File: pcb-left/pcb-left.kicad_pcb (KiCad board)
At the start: 2 copper layers, 138.1 x 95.3 mm, 80 parts, among them SW1 SW_Push, U1 ATmega32U4-AU, Y1 16MHz

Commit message: finished left side pcb
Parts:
- moved C3 1.08 mm to (97.2, 125.4)
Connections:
- U1 pad 10: Net-(U1-Pad10) -> row2
- U1 pad 11: Net-(U1-Pad11) -> row1
- U1 pad 12: Net-(U1-Pad12) -> col6
- U1 pad 18: Net-(U1-Pad18) -> SD+
- U1 pad 19: Net-(U1-Pad19) -> SD-
- U1 pad 20: Net-(U1-Pad20) -> col3
- U1 pad 21: Net-(U1-Pad21) -> col4
- U1 pad 22: Net-(U1-Pad22) -> col5
- U1 pad 29: Net-(U1-Pad29) -> row4
- U1 pad 31: Net-(U1-Pad31) -> col0
- U1 pad 36: Net-(U1-Pad36) -> col2
- U1 pad 37: Net-(U1-Pad37) -> col1
- U1 pad 8: Net-(U1-Pad8) -> row0
- U1 pad 9: Net-(U1-Pad9) -> row3
- USB1 pad 11: Net-(USB1-Pad11) -> +5V
- USB1 pad 13: Net-(USB1-Pad13) -> GND
- USB1 pad 2: Net-(USB1-Pad11) -> +5V
- USB2 pad 13: Net-(USB2-Pad13) -> GND
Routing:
- net +5V: track 129.6 -> 288.2 mm, vias 10 -> 20
- net SD+: track 8.14 -> 118.3 mm, vias 2 -> 9
- net SD-: track 8.11 -> 111.7 mm, vias 2 -> 7
- net col6: track 0.00 -> 92.7 mm, vias 0 -> 9
- net col5: track 67.0 -> 144.6 mm
- net col0: track 85.1 -> 156.9 mm, vias 0 -> 1
- net row0: track 114.4 -> 182.5 mm, vias 0 -> 2
- net col4: track 93.0 -> 142.6 mm
- net row1: track 100.1 -> 146.2 mm, vias 0 -> 4
- net GND: track 331.9 -> 377.7 mm, vias 17 -> 18
- net col1: track 93.9 -> 131.8 mm, vias 0 -> 4
- net col3: track 87.0 -> 114.4 mm, vias 0 -> 1
- net row2: track 102.6 -> 128.7 mm, vias 0 -> 2
- net Net-(USB1-Pad13): track 17.0 -> 0.00 mm
- net col2: track 91.9 -> 106.1 mm, vias 0 -> 2
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- added copper zone on B.Cu, net GND

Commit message: finalized left side pcb
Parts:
- added R9: 10k, Resistor_SMD:R_0805_2012Metric, B.Cu at (96.0, 112.7)
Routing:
- net Net-(R9-Pad2): track 0.00 -> 14.7 mm, vias 0 -> 2
- net +5V: track 288.2 -> 291.2 mm
- added copper zone on B.Cu, net (none)
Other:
- board size 138.1 x 95.3 mm -> 135.7 x 95.2 mm
- board text added: "Split60 by Huskeyboards"

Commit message: added production files for left pcb
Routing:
- net +5V: track 291.2 -> 338.7 mm, vias 20 -> 26
- net GND: track 377.7 -> 365.9 mm

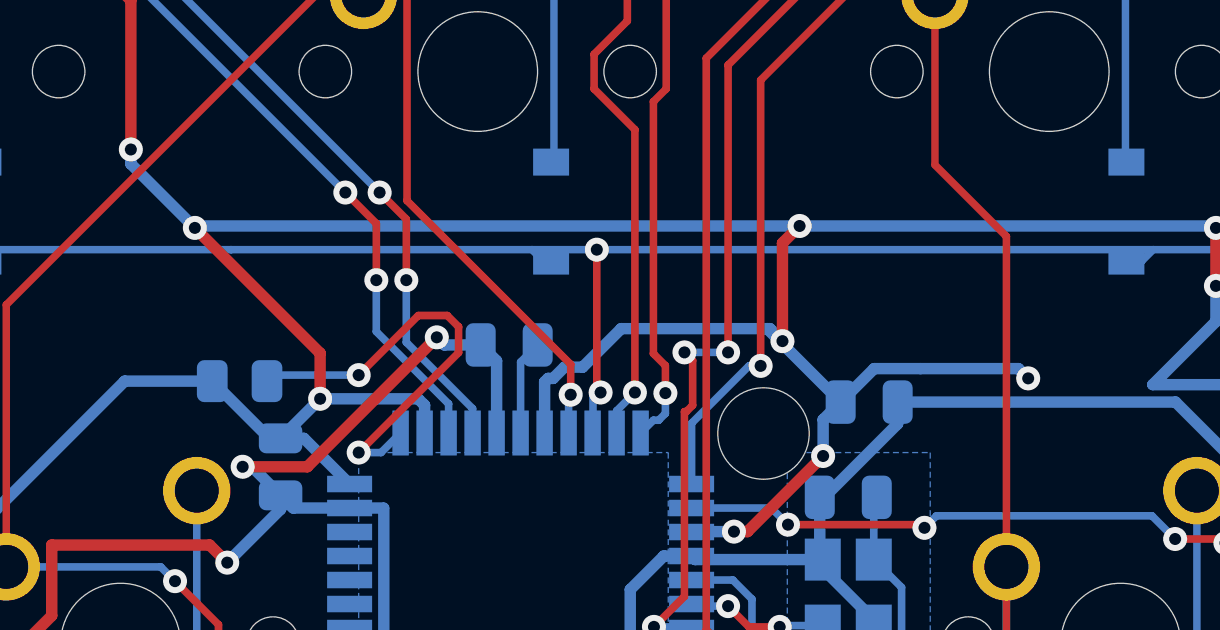
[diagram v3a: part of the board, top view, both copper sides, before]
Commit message: re-zoned crystal area
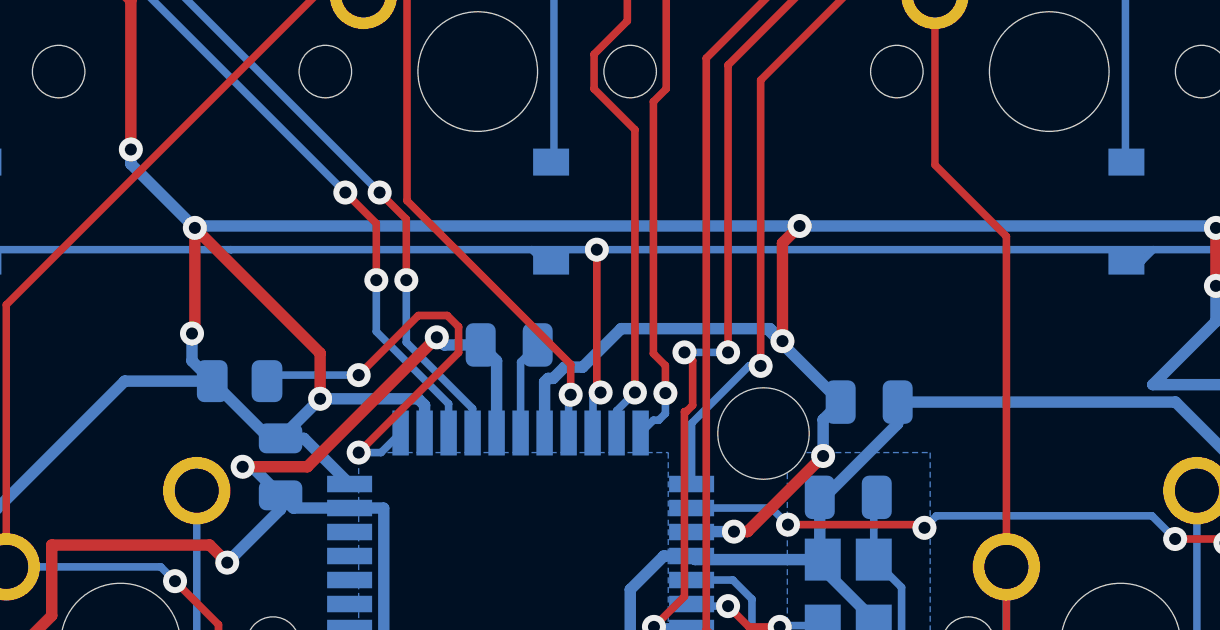
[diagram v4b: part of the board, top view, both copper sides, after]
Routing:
- net +5V: track 338.7 -> 337.2 mm

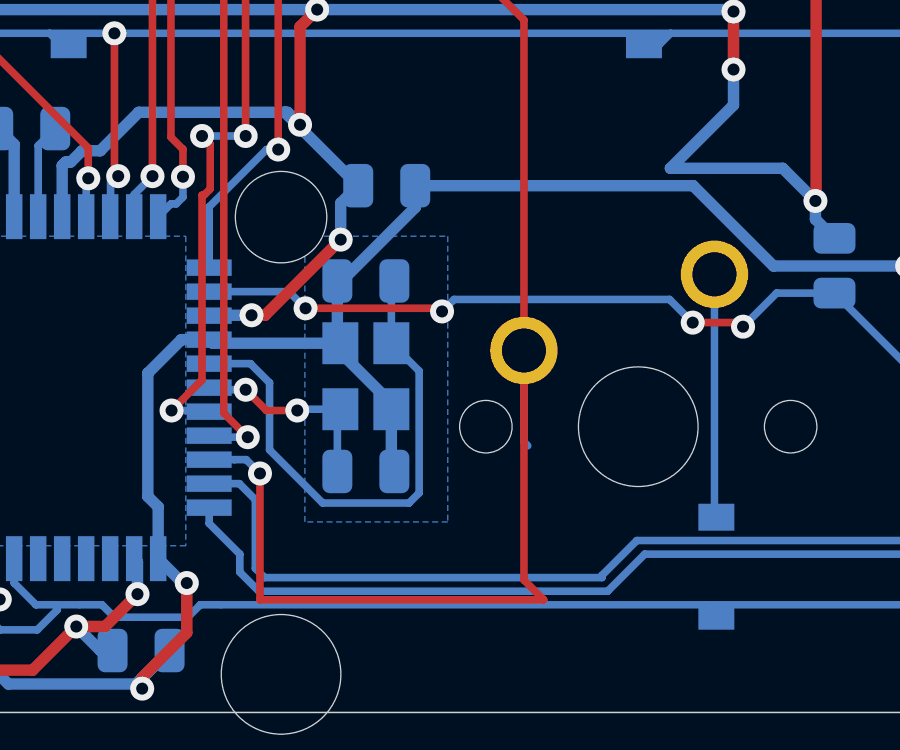
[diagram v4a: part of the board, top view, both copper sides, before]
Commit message: fixed crystal zone
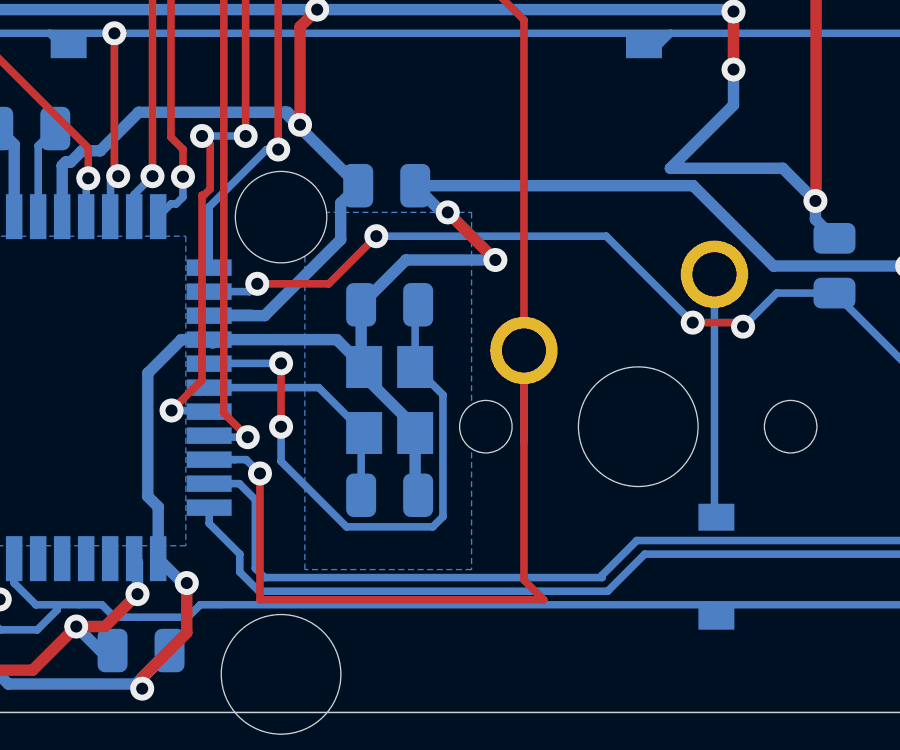
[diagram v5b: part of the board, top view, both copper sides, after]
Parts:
- moved C6 1.12 mm to (117.1, 117.4)
- moved Y1 1.12 mm to (117.1, 120.6)
- moved C5 1.12 mm to (117.1, 123.7)
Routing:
- net GND: track 365.9 -> 371.6 mm, vias 18 -> 20
- net Net-(C6-Pad1): track 17.9 -> 19.5 mm, vias 0 -> 2
- net +5V: track 337.2 -> 338.7 mm, vias 26 -> 24
- net Net-(R7-Pad2): track 39.4 -> 40.6 mm
- net Net-(C5-Pad1): track 6.82 -> 8.01 mm, vias 2 -> 0
